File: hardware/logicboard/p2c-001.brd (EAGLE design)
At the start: 89 x 51 mm, 53 parts, among them IC1 74LS06N, J0 9V, J1 MKR, J11 Qwiic, J2 GPIO, J4 RLY, J5 SPI, J7 DIN5, J9 DIN5, K1 G5V1, Q1 220mA/50V/3.5Ω, Q2 220mA/50V/3.5Ω, T1 2SC1815, U1 DS18B20

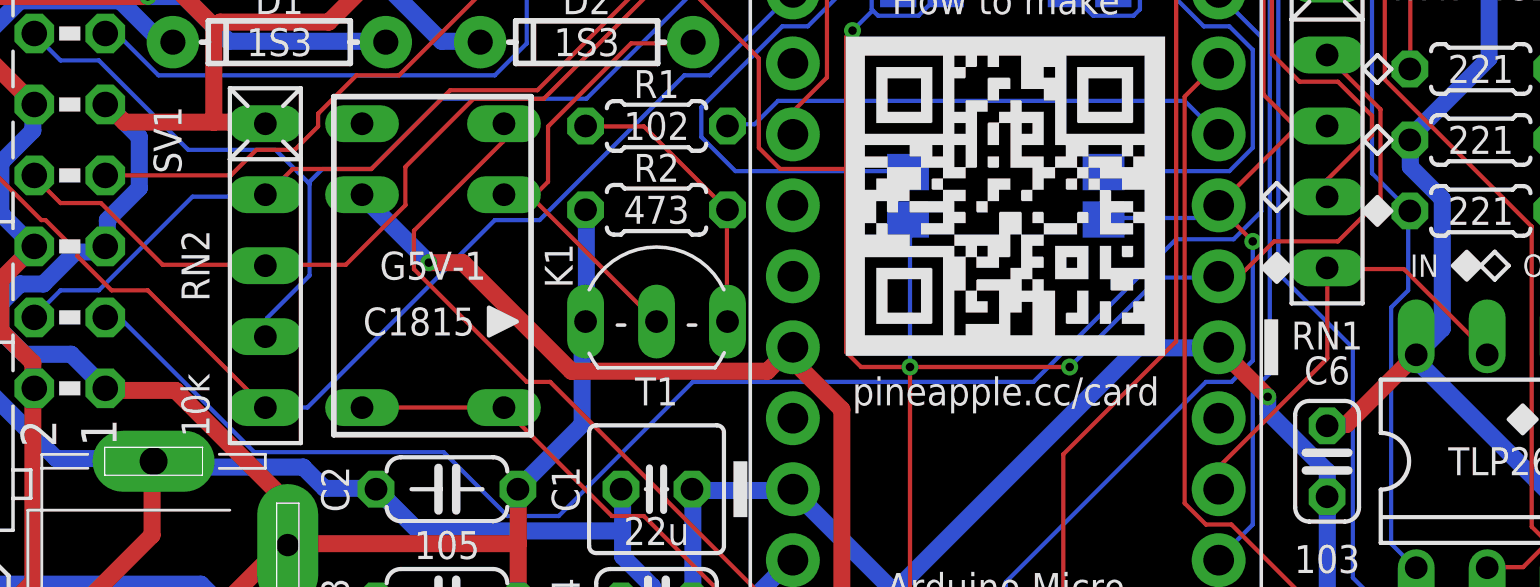
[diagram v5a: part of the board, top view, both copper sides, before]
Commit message: Swapped RN1 and RN2.
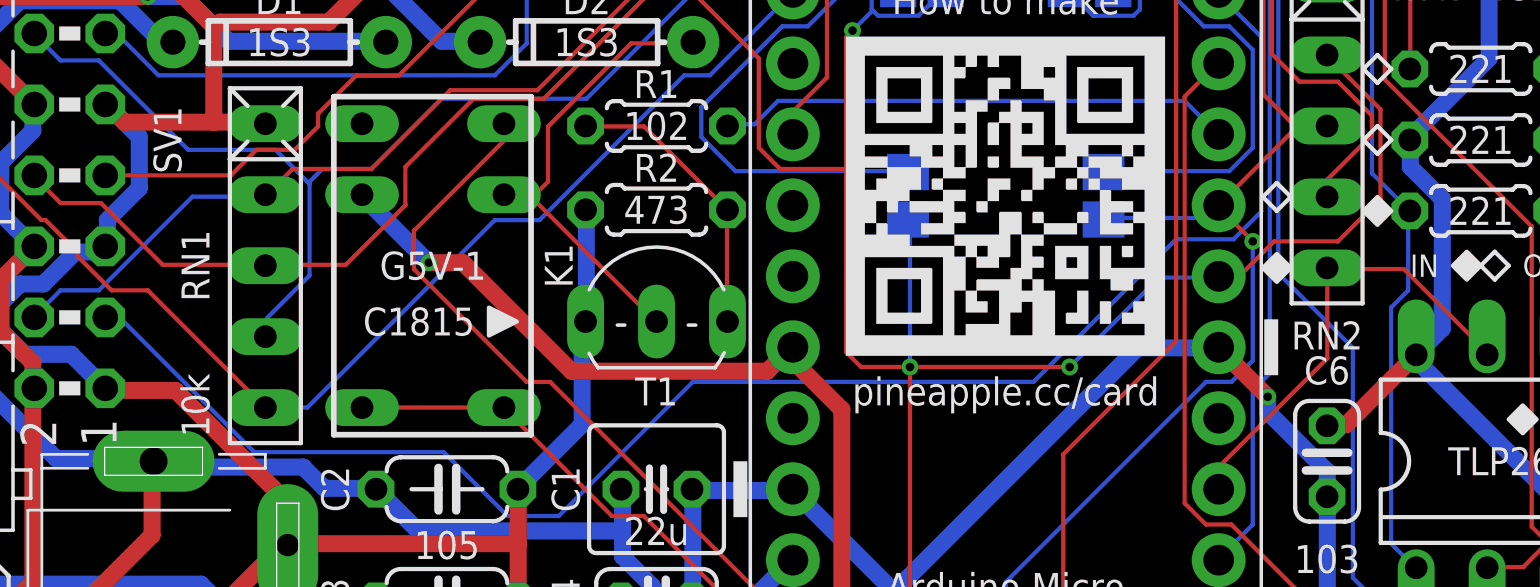
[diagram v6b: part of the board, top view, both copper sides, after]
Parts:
- RN1: value 4.7k -> 10k
- RN2: value 10k -> 4.7k
- moved RN1 38.3 mm to (18.0, 21.0)
- moved RN2 38.3 mm to (56.0, 26.0)
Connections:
- net ANLG1: now also RN1.2; no longer RN2.2
- net ANLG2: now also RN1.3; no longer RN2.3
- net ANLG3: now also RN1.4; no longer RN2.4
- net ANLG4: now also RN1.5; no longer RN2.5
- net GND: now also RN1.1; no longer RN2.1
- net NMORTN: now also RN2.4; no longer RN1.4
- net RX: now also RN2.5; no longer RN1.5
- net SCL: now also RN2.3; no longer RN1.3
- net SDA: now also RN2.2; no longer RN1.2
- net VCC: now also RN2.1; no longer RN1.1
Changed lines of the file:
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@@
 <attribute name="VALUE" x="42.849" y="3.587" size="0.6096" layer="28" font="vector" ratio="20" rot="MR180"/>
 </element>
-<element name="RN2" library="resistor-net" library_urn="urn:adsk.eagle:library:343" package="RN-5" package3d_urn="urn:adsk.eagle:package:24976/1" value="10k" x="18" y="21" smashed="yes" rot="R270">
+<element name="RN1" library="resistor-net" library_urn="urn:adsk.eagle:library:343" package="RN-5" package3d_urn="urn:adsk.eagle:package:24976/1" value="10k" x="18" y="21" smashed="yes" rot="R270">
 <attribute name="MF" value="" x="18" y="21" size="1.778" layer="27" rot="R270" display="off"/>
 <attribute name="MPN" value="" x="18" y="21" size="1.778" layer="27" rot="R270" display="off"/>
@@
 <attribute name="VALUE" x="45.46" y="22.865" size="1.27" layer="28" rot="MR90"/>
 </element>
-<element name="RN1" library="resistor-net" library_urn="urn:adsk.eagle:library:343" package="RN-5" package3d_urn="urn:adsk.eagle:package:24976/1" value="4.7k" x="56" y="26" smashed="yes" rot="R270">
+<element name="RN2" library="resistor-net" library_urn="urn:adsk.eagle:library:343" package="RN-5" package3d_urn="urn:adsk.eagle:package:24976/1" value="4.7k" x="56" y="26" smashed="yes" rot="R270">
 <attribute name="MF" value="" x="56" y="26" size="1.778" layer="27" rot="R270" display="off"/>
 <attribute name="MPN" value="" x="56" y="26" size="1.778" layer="27" rot="R270" display="off"/>
@@
 <contactref element="U$2" pad="P$12"/>
 <contactref element="L2" pad="K"/>
-<contactref element="RN2" pad="1"/>
+<contactref element="RN1" pad="1"/>
 <contactref element="U$2" pad="P$21"/>
 <contactref element="J11" pad="1"/>
@@
 <contactref element="J1" pad="5"/>
 <contactref element="U1" pad="3"/>
-<contactref element="RN1" pad="1"/>
+<contactref element="RN2" pad="1"/>
 <contactref element="IC1" pad="14"/>
 <contactref element="JP1" pad="3"/>
@@
 <contactref element="U$2" pad="P$31"/>
 <contactref element="SV1" pad="4"/>
-<contactref element="RN2" pad="2"/>
+<contactref element="RN1" pad="2"/>
 <wire x1="15.3924" y1="23.4696" x2="17.9832" y2="23.4696" width="0.1524" layer="16"/>
 <wire x1="12.0396" y1="20.1168" x2="15.3924" y2="23.4696" width="0.1524" layer="16"/>
@@
 <contactref element="U$2" pad="P$30"/>
 <contactref element="SV1" pad="8"/>
-<contactref element="RN2" pad="3"/>
+<contactref element="RN1" pad="3"/>
 <wire x1="14.3256" y1="21.0312" x2="17.9832" y2="21.0312" width="0.1524" layer="1"/>
 <wire x1="12.1158" y1="23.241" x2="14.3256" y2="21.0312" width="0.1524" layer="1"/>
@@
 <contactref element="U$2" pad="P$29"/>
 <contactref element="SV1" pad="12"/>
-<contactref element="RN2" pad="4"/>
+<contactref element="RN1" pad="4"/>
 <wire x1="18.0594" y1="19.1262" x2="18.0594" y2="18.5166" width="0.1524" layer="16"/>
 <wire x1="19.5834" y1="20.6502" x2="18.0594" y2="19.1262" width="0.1524" layer="16"/>
@@
 <contactref element="U$2" pad="P$28"/>
 <contactref element="SV1" pad="16"/>
-<contactref element="RN2" pad="5"/>
+<contactref element="RN1" pad="5"/>
 <wire x1="19.5072" y1="15.9258" x2="18.0594" y2="15.9258" width="0.1524" layer="16"/>
 <wire x1="26.2128" y1="22.6314" x2="19.5072" y2="15.9258" width="0.1524" layer="16"/>
@@
 <contactref element="J1" pad="3"/>
 <contactref element="JP2" pad="4"/>
-<contactref element="RN1" pad="3"/>
+<contactref element="RN2" pad="3"/>
 <wire x1="46.4058" y1="34.671" x2="46.4058" y2="35.9664" width="0.1524" layer="16"/>
 <wire x1="49.3014" y1="31.7754" x2="49.0347" y2="32.0421" width="0.1524" layer="16"/>
@@
 <contactref element="J1" pad="2"/>
 <contactref element="JP2" pad="5"/>
-<contactref element="RN1" pad="2"/>
+<contactref element="RN2" pad="2"/>
 <wire x1="57.912" y1="26.5938" x2="56.007" y2="28.4988" width="0.1524" layer="1"/>
 <wire x1="57.912" y1="23.3934" x2="57.912" y2="26.5938" width="0.1524" layer="1"/>
@@
 <signal name="RX">
 <contactref element="U$2" pad="P$14"/>
-<contactref element="RN1" pad="5"/>
+<contactref element="RN2" pad="5"/>
 <contactref element="OK1" pad="7"/>
 <wire x1="58.7502" y1="20.8788" x2="56.007" y2="20.8788" width="0.1524" layer="1"/>
@@
 <signal name="NMORTN">
 <contactref element="IC1" pad="2"/>
-<contactref element="RN1" pad="4"/>
+<contactref element="RN2" pad="4"/>
 <contactref element="IC1" pad="3"/>
 <wire x1="56.007" y1="24.0792" x2="56.007" y2="23.4696" width="0.1524" layer="1"/>

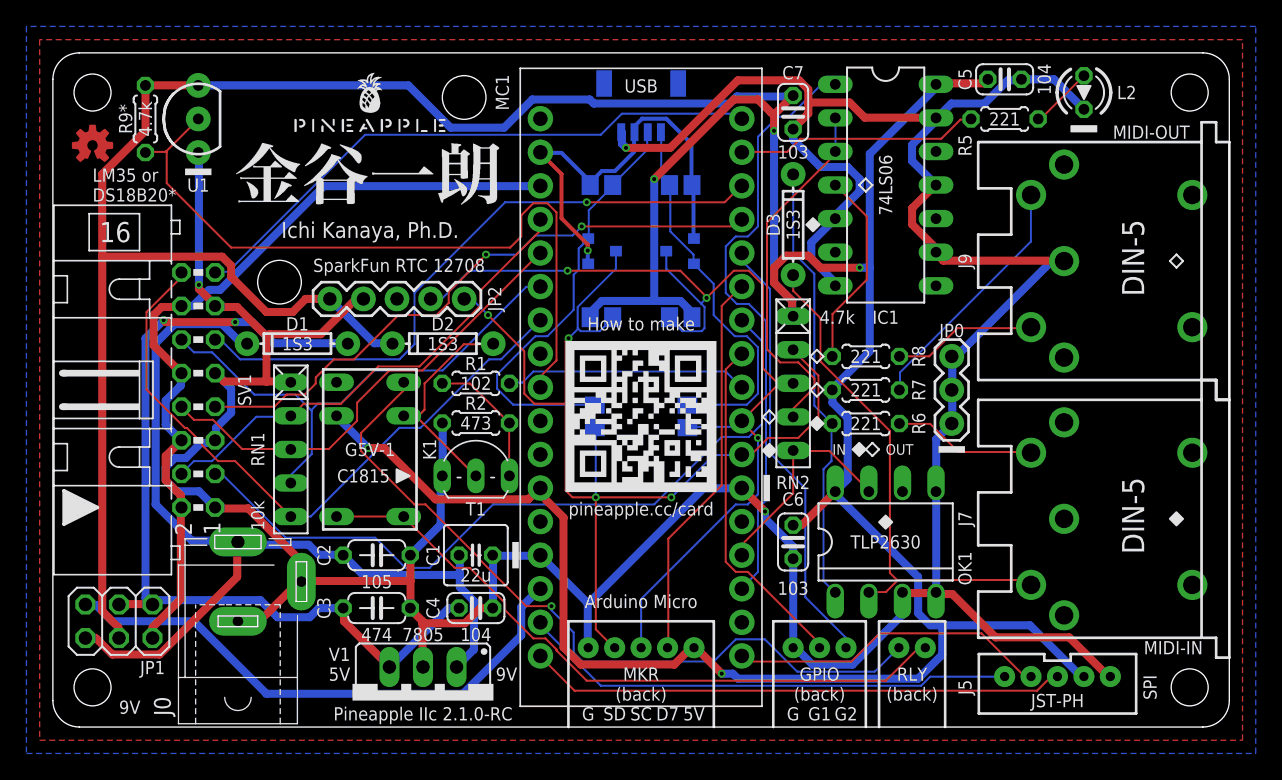
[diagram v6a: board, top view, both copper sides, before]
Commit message: Changed width of signal patterns.
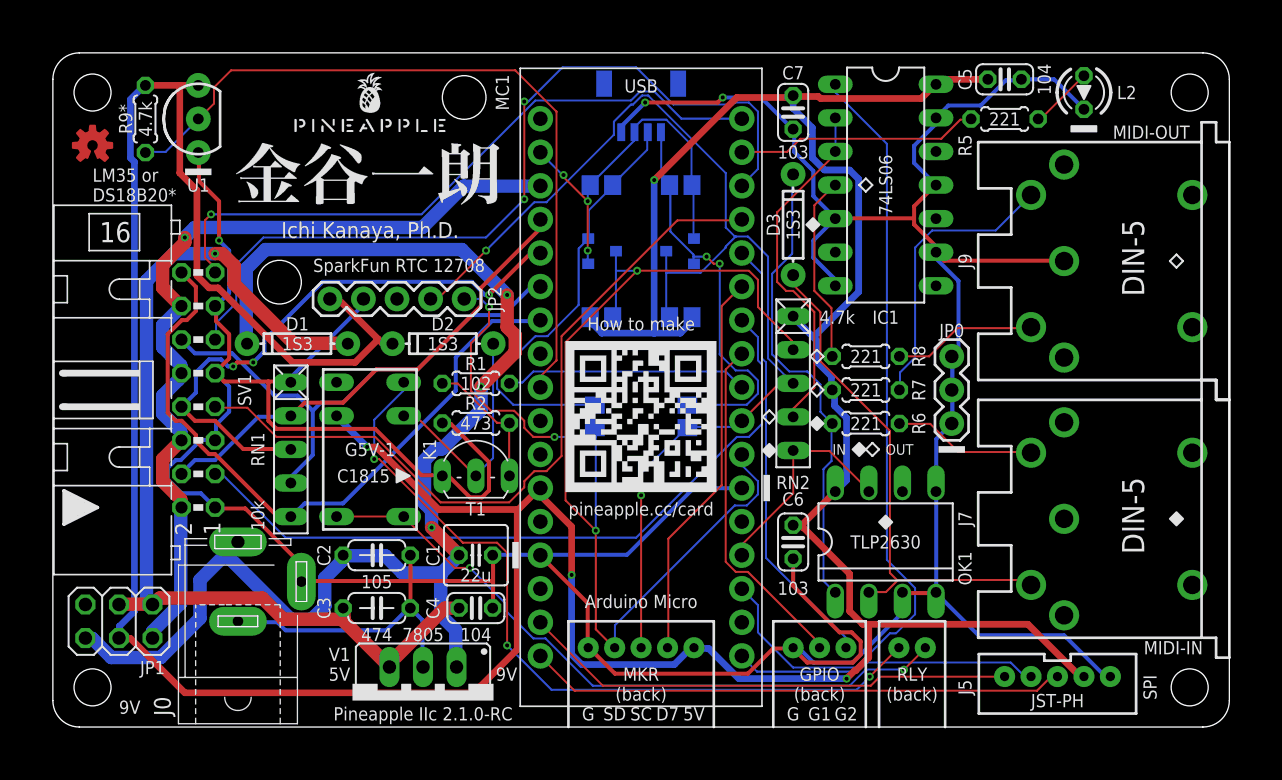
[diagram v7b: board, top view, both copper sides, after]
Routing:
- net VIN: track 41.8 -> 0.00 mm
- net GND: track 291.2 -> 321.6 mm
- net V+: track 72.1 -> 100.9 mm, vias 0 -> 3
- net SDA: track 80.8 -> 103.1 mm
- net DTCT3: track 48.2 -> 64.0 mm, vias 1 -> 2
- net TX: track 45.8 -> 61.1 mm
- net DTCT2: track 46.5 -> 57.3 mm, vias 2 -> 0
- net SCL: track 79.4 -> 89.4 mm, vias 3 -> 2
- net ANLG2: track 35.5 -> 44.2 mm, vias 0 -> 3
- net VCC: track 316.4 -> 308.6 mm, vias 5 -> 4
- net VOUT: track 68.0 -> 75.4 mm, vias 2 -> 1
- net DTCT4: track 45.0 -> 49.8 mm, vias 0 -> 1
- net VDD: track 33.9 -> 29.6 mm, vias 1 -> 3
- net VCC/2: track 61.5 -> 64.6 mm, vias 0 -> 1
- net MOSND: track 18.9 -> 21.7 mm
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- removed copper zone on layer 1, net GND
- removed copper zone on layer 16, net GND

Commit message: Changed width of patterns.
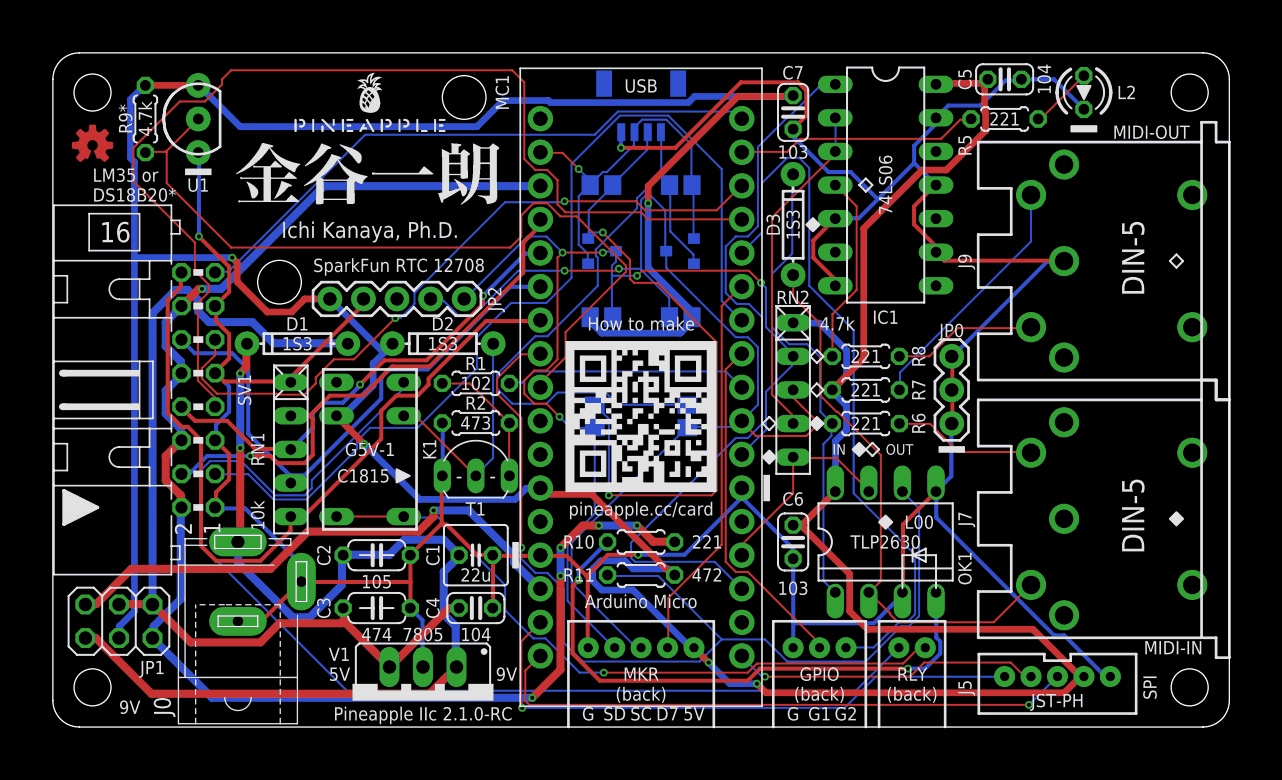
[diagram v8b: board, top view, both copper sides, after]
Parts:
- added R10: 220, resistor:0204/5
- added R11: 4.7k, resistor:0204/5
- moved RN2 0.50 mm to (56.0, 25.5)
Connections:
- new net MNTRA: OK1.4, R10.1
- net GND: no longer OK1.4
- net MNTR: now also OK1.6, R11.1
- net VCC: now also R11.2
- net VCC/2: now also R10.2
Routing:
- net MNTR: track 0.00 -> 77.6 mm, vias 0 -> 1
- net VCC/2: track 64.6 -> 112.6 mm, vias 1 -> 6
- net MNTRA: track 0.00 -> 43.8 mm, vias 0 -> 2
- net GND: track 321.6 -> 280.7 mm
- net VIN: track 0.00 -> 40.4 mm, vias 0 -> 1
- net RLYA: track 59.1 -> 85.2 mm, vias 3 -> 0
- net DTCT2: track 57.3 -> 80.6 mm
- net V+: track 100.9 -> 79.4 mm, vias 3 -> 2
- net GPIO2: track 33.1 -> 53.9 mm
- net SCL3V: track 30.5 -> 49.4 mm, vias 2 -> 0
- net SDA: track 103.1 -> 84.4 mm, vias 4 -> 5
- net SDA3V: track 32.6 -> 50.7 mm, vias 0 -> 2
- net DTCT1: track 55.4 -> 71.7 mm
- net VCC: track 308.6 -> 322.2 mm, vias 4 -> 5
- net DTCT3: track 64.0 -> 52.6 mm
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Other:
- board text added: "472"
- board text added: "L00"
